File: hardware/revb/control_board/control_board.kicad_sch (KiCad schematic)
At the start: 0 parts

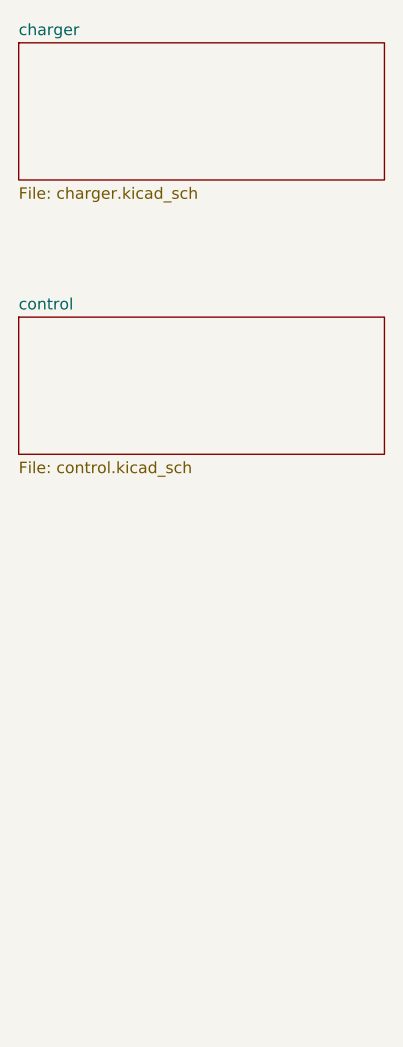
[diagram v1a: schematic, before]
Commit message: Rev B control board: redraw schematic with wires (4 sheets), review fixes
- wire/power-symbol style, netlist checked against intended nets, KiCad 9 ERC 0/0
- 2N7002 symbol pin order (GSD), TDSON-8 FET symbol, 60V FETs, 50V output caps
- NODE TVS, comparator hysteresis, EN_PMOS 4.7k, aux input 10R, CAN term (DNP)
- ISNS offset sink (DAC) for adjustable input-power limit; ICAP_S moved to PA6
- old label-only sheets moved to _superseded/

Co-Authored-By: Claude Opus 5.5 <noreply@anthropic.com>
Claude-Session: https://claude.ai/code/session_0144JDnT2EZoCv7WaMs1JYhQ
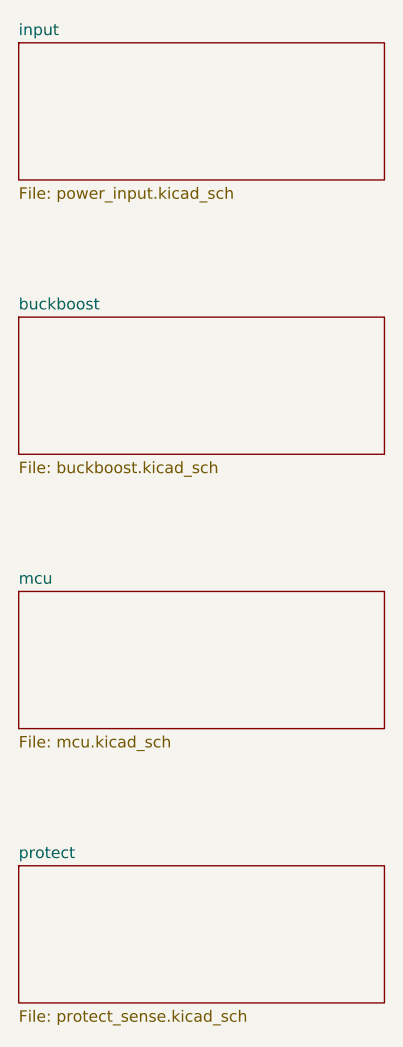
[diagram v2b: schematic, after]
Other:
- removed sheet charger
- removed sheet control
- added sheet buckboost (buckboost.kicad_sch)
- added sheet input (power_input.kicad_sch)
- added sheet mcu (mcu.kicad_sch)
- added sheet protect (protect_sense.kicad_sch)
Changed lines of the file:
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@@
 (title_block (title "Rev B control board (root)"))
 (sheet (at 30.48 30.48) (size 40.64 15.24) (fields_autoplaced) (stroke (width 0.1524) (type solid)) (fill (color 0 0 0 0.0))
-(property "Sheetname" "charger" (at 30.48 29.78 0) (effects (font (size 1.27 1.27)) (justify left bottom)))
-(property "Sheetfile" "charger.kicad_sch" (at 30.48 46.48 0) (effects (font (size 1.27 1.27)) (justify left top)))
-(instances (project "control_board" (path "/9282d039-0d09-446f-9346-c13d805184d5" (page "2"))))
+(property "Sheetname" "input" (at 30.48 29.78 0) (effects (font (size 1.27 1.27)) (justify left bottom)))
+(property "Sheetfile" "power_input.kicad_sch" (at 30.48 46.48 0) (effects (font (size 1.27 1.27)) (justify left top)))
+(instances (project "control_board" (path "/88307719-d61f-4546-bf4c-258b512304c2" (page "2"))))
 )
 (sheet (at 30.48 60.96) (size 40.64 15.24) (fields_autoplaced) (stroke (width 0.1524) (type solid)) (fill (color 0 0 0 0.0))
-(property "Sheetname" "control" (at 30.48 60.26 0) (effects (font (size 1.27 1.27)) (justify left bottom)))
-(property "Sheetfile" "control.kicad_sch" (at 30.48 76.96 0) (effects (font (size 1.27 1.27)) (justify left top)))
-(instances (project "control_board" (path "/9282d039-0d09-446f-9346-c13d805184d5" (page "3"))))
+(property "Sheetname" "buckboost" (at 30.48 60.26 0) (effects (font (size 1.27 1.27)) (justify left bottom)))
+(property "Sheetfile" "buckboost.kicad_sch" (at 30.48 76.96 0) (effects (font (size 1.27 1.27)) (justify left top)))
+(instances (project "control_board" (path "/88307719-d61f-4546-bf4c-258b512304c2" (page "3"))))
+)
+(sheet (at 30.48 91.44) (size 40.64 15.24) (fields_autoplaced) (stroke (width 0.1524) (type solid)) (fill (color 0 0 0 0.0))
+(property "Sheetname" "mcu" (at 30.48 90.74 0) (effects (font (size 1.27 1.27)) (justify left bottom)))
+(property "Sheetfile" "mcu.kicad_sch" (at 30.48 107.44 0) (effects (font (size 1.27 1.27)) (justify left top)))
+(instances (project "control_board" (path "/88307719-d61f-4546-bf4c-258b512304c2" (page "4"))))
+)
+(sheet (at 30.48 121.92) (size 40.64 15.24) (fields_autoplaced) (stroke (width 0.1524) (type solid)) (fill (color 0 0 0 0.0))
+(property "Sheetname" "protect" (at 30.48 121.22 0) (effects (font (size 1.27 1.27)) (justify left bottom)))
+(property "Sheetfile" "protect_sense.kicad_sch" (at 30.48 137.92 0) (effects (font (size 1.27 1.27)) (justify left top)))
+(instances (project "control_board" (path "/88307719-d61f-4546-bf4c-258b512304c2" (page "5"))))
 )
 (sheet_instances (path "/" (page "1")))
